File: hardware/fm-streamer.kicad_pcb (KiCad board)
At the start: 4 copper layers, 40 x 60 mm, 56 parts, among them J1 USB_A, U1 ESP32_DevKit_V1_DOIT, U2 PCM1772PWR, U3 SI4721

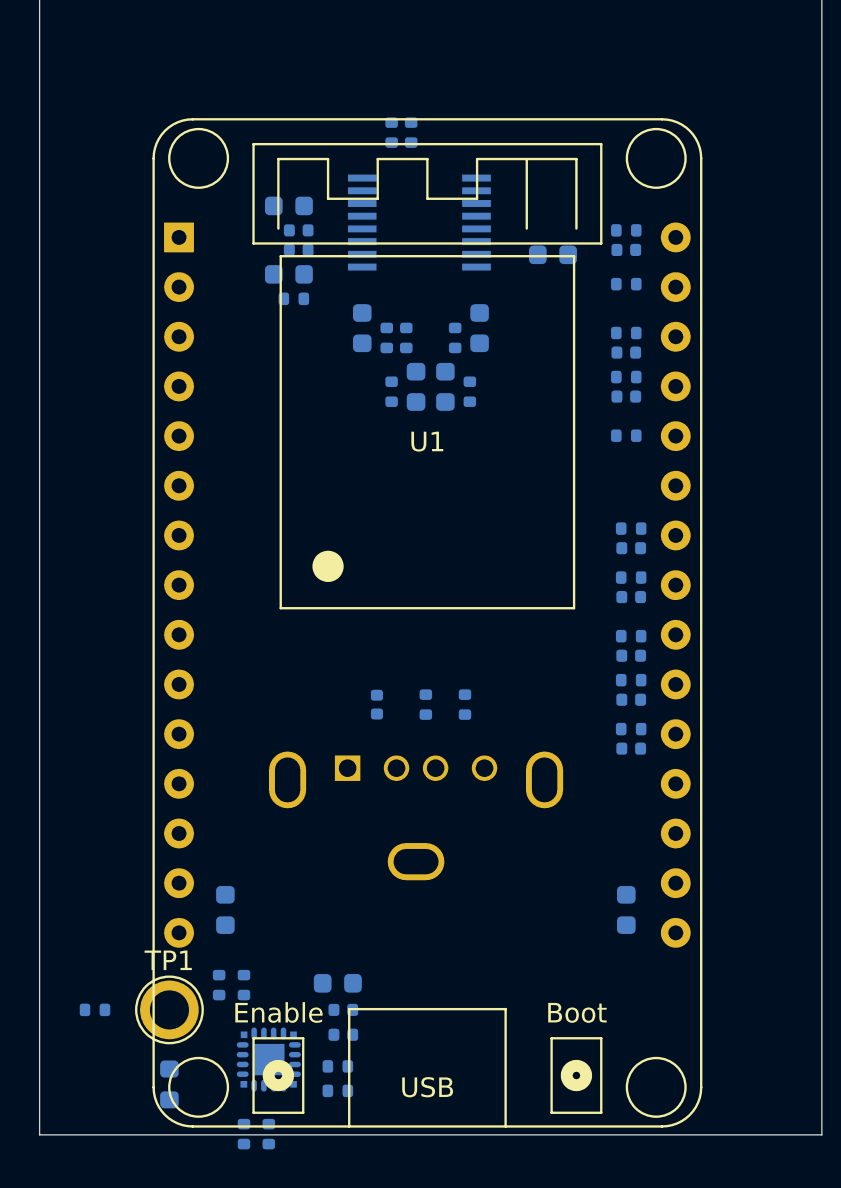
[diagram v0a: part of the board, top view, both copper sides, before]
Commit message: cleaning up routing
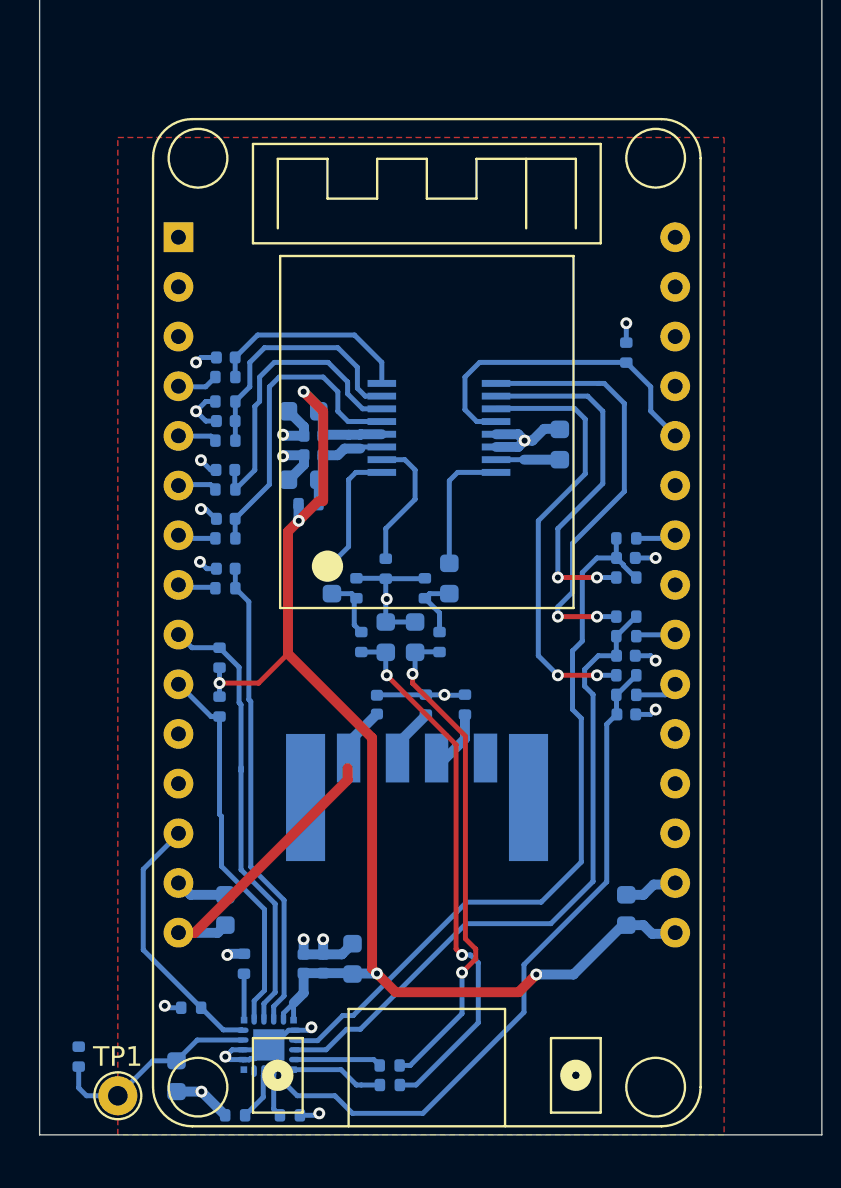
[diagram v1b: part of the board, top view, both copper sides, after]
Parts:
- added R28: 0, Resistor_SMD:R_0402_1005Metric, B.Cu at (210.0, 106.5)
- added R29: 0, Resistor_SMD:R_0402_1005Metric, B.Cu at (210.0, 101.5)
- added R30: 0, Resistor_SMD:R_0402_1005Metric, B.Cu at (210.0, 103.5)
- J1: footprint Connector_USB:USB_A_Molex_105057_Vertical -> Connector_USB:USB_A_Plug_Molex_0480371000_90_deg_mount
- TP1: footprint TestPoint:TestPoint_Plated_Hole_D2.0mm -> TestPoint:TestPoint_THTPad_D2.0mm_Drill1.0mm
- moved R12 30.0 mm to (189.2, 108.1), turned to 90 degrees
- moved R9 25.9 mm to (189.5, 99.5), turned to 180 degrees
- moved C9 24.7 mm to (189.5, 98.5), turned to 180 degrees
- moved R3 23.7 mm to (189.2, 105.6), turned to 270 degrees
- moved R7 23.2 mm to (189.5, 102.0), turned to 180 degrees
- moved C11 22.6 mm to (189.5, 93.5), turned to 180 degrees
- moved C7 22.3 mm to (189.5, 101.0), turned to 180 degrees
- moved R11 21.9 mm to (189.5, 94.5), turned to 180 degrees
- moved C10 21.1 mm to (189.5, 96.0), turned to 180 degrees
- moved R10 20.8 mm to (189.5, 97.0), turned to 180 degrees
- moved R8 20.6 mm to (189.5, 91.2), turned to 180 degrees
- moved C8 20.5 mm to (189.5, 90.2), turned to 180 degrees
- moved R16 16.2 mm to (189.5, 92.5), turned to 180 degrees
- moved R15 15.7 mm to (210.0, 90.0)
- moved C19 12.9 mm to (200.9, 101.5)
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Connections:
- C11 pad 1: SPI_CS -> SPI_~CS~
- R11 pad 1: SPI_CS -> SPI_~CS~
- R12 pad 1: I2C_SCK -> I2C_SCL
- U1 pad 10: DAC_~RST~ -> I2C_SCL
- U1 pad 13: Net-(U1-Pad13) -> RADIO_~RST~
- U1 pad 20: /I2S_DCLK_R -> Net-(U1-Pad20)
- U1 pad 21: /I2S_DATA_R -> /I2S_DCLK_R
- U1 pad 23: /SPI_CS_R -> Net-(U1-Pad23)
- U1 pad 24: /SPI_CLK_R -> /I2S_DATA_R
- U1 pad 26: I2C_SDA -> DAC_~RST~
- U1 pad 27: /RAD_CLK_R -> Net-(U1-Pad27)
- U1 pad 28: /DAC_CLK_R -> Net-(U1-Pad28)
- U1 pad 29: I2C_SCK -> Net-(U1-Pad29)
- U1 pad 30: /SPI_MOSI_R -> Net-(U1-Pad30)
- U1 pad 4: Net-(U1-Pad4) -> /DAC_CLK_R
- U1 pad 5: Net-(U1-Pad5) -> /SPI_CS_R
- U1 pad 6: Net-(U1-Pad6) -> /SPI_CLK_R
- U1 pad 7: Net-(U1-Pad7) -> /SPI_MOSI_R
- U1 pad 8: RADIO_~RST~ -> /RAD_CLK_R
- U1 pad 9: Net-(U1-Pad9) -> I2C_SDA
- U2 pad 1: I2S_WCLK -> Net-(R30-Pad1)
- U2 pad 2: I2S_DATA -> Net-(R29-Pad1)
- U2 pad 3: I2S_DCLK -> Net-(R28-Pad1)
- U3 pad 7: I2C_SCK -> I2C_SCL
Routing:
- net +3V3: track 0.00 -> 69.7 mm, vias 0 -> 5
- net GND: track 0.00 -> 56.4 mm, vias 0 -> 22
- net I2S_DATA: track 0.00 -> 38.1 mm
- net I2S_DCLK: track 0.00 -> 35.3 mm
- net I2S_WCLK: track 0.00 -> 34.2 mm
- net AUDIO_L: track 0.00 -> 27.7 mm, vias 0 -> 2
- net AUDIO_R: track 0.00 -> 26.1 mm, vias 0 -> 2
- net RADIO_REFCLK: track 0.00 -> 24.3 mm
- net I2C_SDA: track 0.00 -> 22.9 mm
- net Net-(R30-Pad1): track 0.00 -> 22.3 mm, vias 0 -> 2
- net Net-(R28-Pad1): track 0.00 -> 22.3 mm, vias 0 -> 2
- net I2C_SCL: track 0.00 -> 19.4 mm
- net +5V: track 0.00 -> 18.4 mm
- net Net-(R29-Pad1): track 0.00 -> 18.2 mm, vias 0 -> 2
- net DAC_~RST~: track 0.00 -> 16.9 mm
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- added copper zone on F.Cu, net GND
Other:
- copper layers 4 -> 2

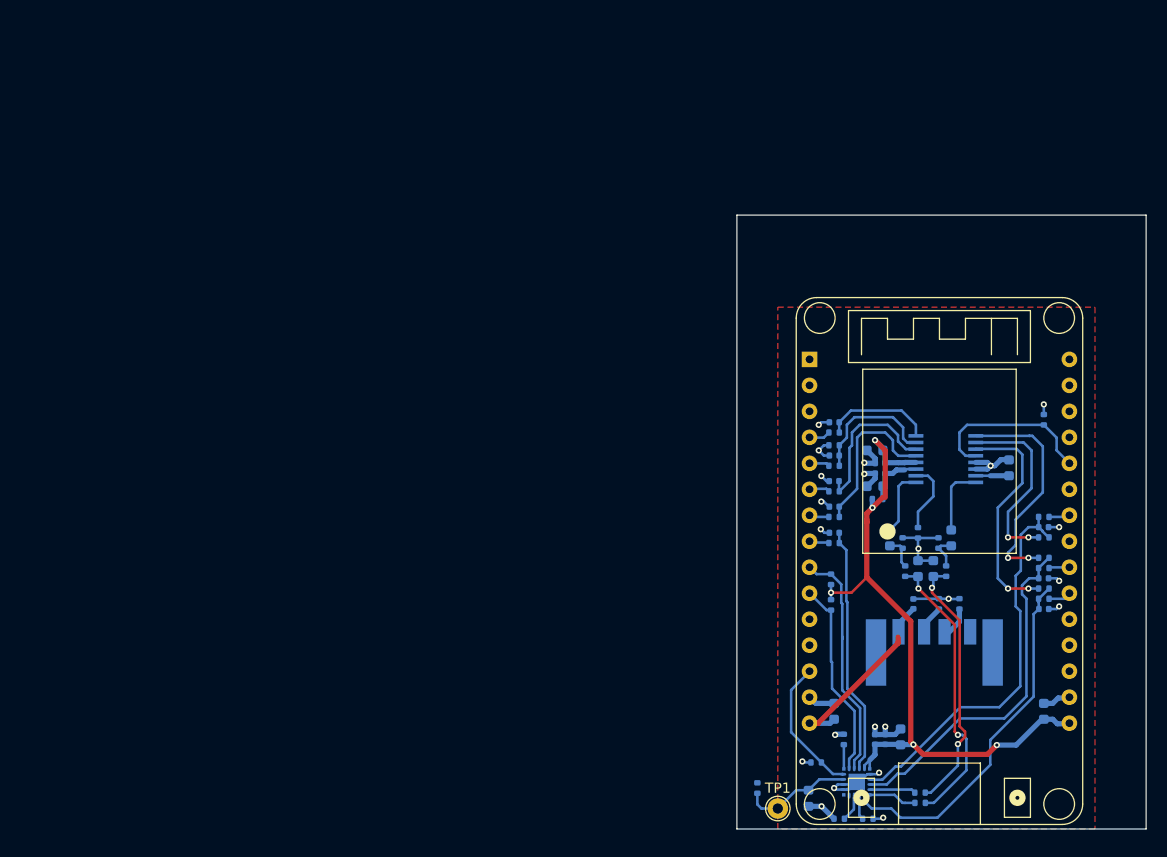
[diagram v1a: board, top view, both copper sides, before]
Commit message: added 3D body for Molex USB connector, layout cleanup
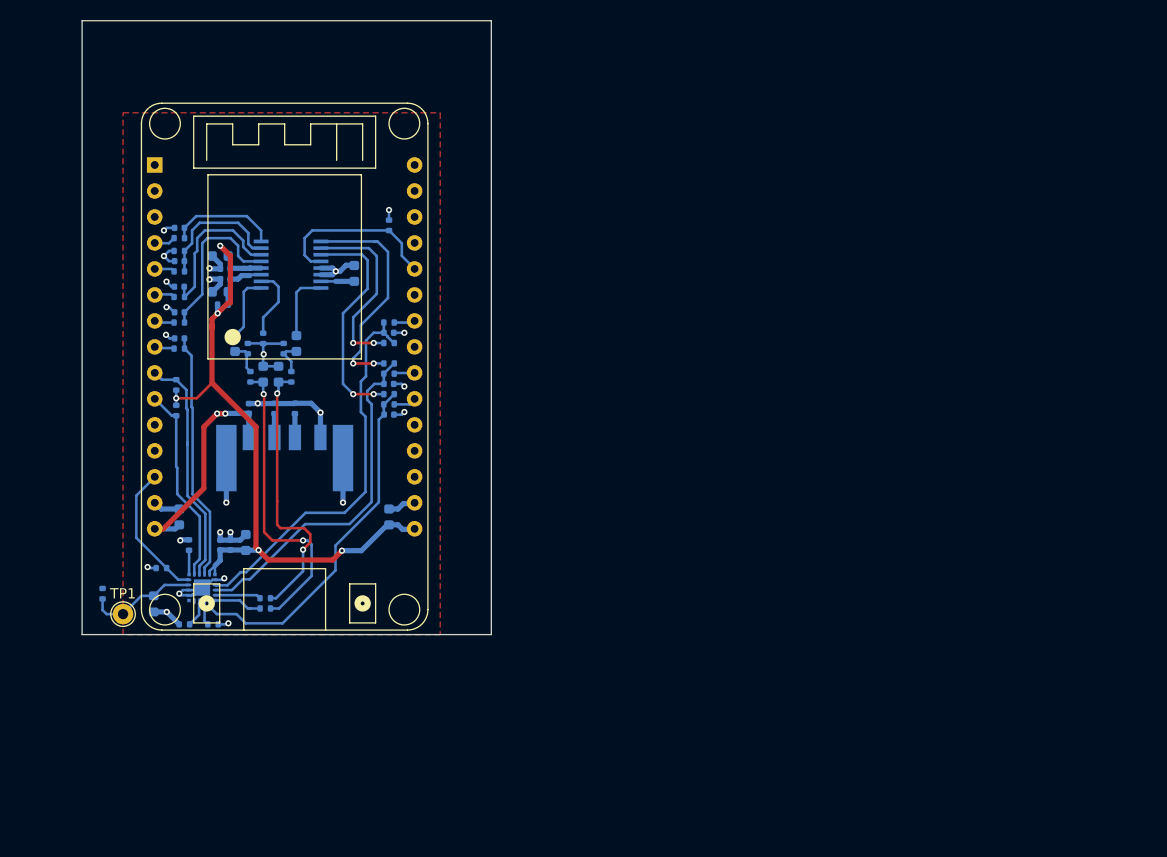
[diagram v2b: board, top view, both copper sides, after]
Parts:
- moved C1 67.7 mm to (132.3, 88.9)
- moved R1 67.7 mm to (136.8, 88.9)
- moved R2 67.7 mm to (134.8, 88.9)
- moved C11 66.8 mm to (125.5, 74.5)
- moved C7 66.8 mm to (125.5, 82.0)
- moved C8 66.8 mm to (125.5, 71.2)
- moved C9 66.8 mm to (125.5, 79.5)
- moved C10 66.8 mm to (125.5, 77.0)
- moved C12 66.8 mm to (129.5, 77.5)
- moved C13 66.8 mm to (130.0, 76.2)
- moved C14 66.8 mm to (129.5, 74.0)
- moved C15 66.8 mm to (130.0, 75.2)
- moved C16 66.8 mm to (142.6, 75.7)
- moved C17 66.8 mm to (129.5, 102.2)
- moved C18 66.8 mm to (130.5, 102.2)
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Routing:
- net GND: track 56.4 -> 70.8 mm, vias 22 -> 25
- net +5V: track 18.4 -> 22.8 mm, vias 0 -> 2
- net AUDIO_L: track 27.7 -> 29.5 mm
- net AUDIO_R: track 26.1 -> 27.4 mm
- net Net-(J1-Pad3): track 3.36 -> 2.32 mm
- net Net-(J1-Pad2): track 3.36 -> 2.32 mm

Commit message: ready for fab quote
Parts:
- added J1 (x2): USB_A, Connector_USB:USB_A_Plug_Molex_0480371000_90_deg_mount, B.Cu at (129.7, 102.4)
- moved R14 12.7 mm to (111.7, 118.0), turned to 135 degrees
- moved J1 11.2 mm to (129.7, 102.4)
- moved U1 11.2 mm to (129.7, 74.5)
- moved R12 11.2 mm to (119.1, 98.5)
- moved R19 11.2 mm to (120.3, 111.7)
- moved R3 11.2 mm to (119.1, 96.0)
- moved R1 11.2 mm to (130.7, 98.3)
- moved R2 11.2 mm to (128.7, 98.3)
- moved C10 11.2 mm to (119.4, 86.4)
- moved C11 11.2 mm to (119.4, 83.9)
- moved C12 11.2 mm to (123.4, 86.9)
- moved C13 11.2 mm to (123.9, 85.7)
- moved C14 11.2 mm to (123.4, 83.4)
- moved C15 11.2 mm to (123.9, 84.7)
- moved C19 11.2 mm to (130.8, 92.0)
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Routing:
- net /ANTENNA: track 0.00 -> 144.4 mm
- net GND: track 70.8 -> 97.5 mm, vias 25 -> 89
- net AUDIO_R: track 27.4 -> 23.7 mm
- net AUDIO_L: track 29.5 -> 26.6 mm
- net RADIO_~RST~: track 13.5 -> 15.0 mm
- net +5V: track 22.8 -> 24.3 mm
- net Net-(L1-Pad1): track 10.8 -> 9.43 mm
- net RADIO_REFCLK: track 24.3 -> 25.2 mm
- net I2S_DCLK: track 35.3 -> 36.2 mm
- net Net-(R29-Pad1): track 18.2 -> 18.9 mm
- net I2C_SDA: track 22.9 -> 23.6 mm
- net Net-(R30-Pad1): track 22.3 -> 21.7 mm
- added copper zone on B.Cu, net GND
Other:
- board size 40 x 60 mm -> 39.4 x 57.2 mm
- board text added: "ANT"
- board text added: "FM STREAMER REV0"
